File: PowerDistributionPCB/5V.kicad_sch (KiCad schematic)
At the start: 1 part

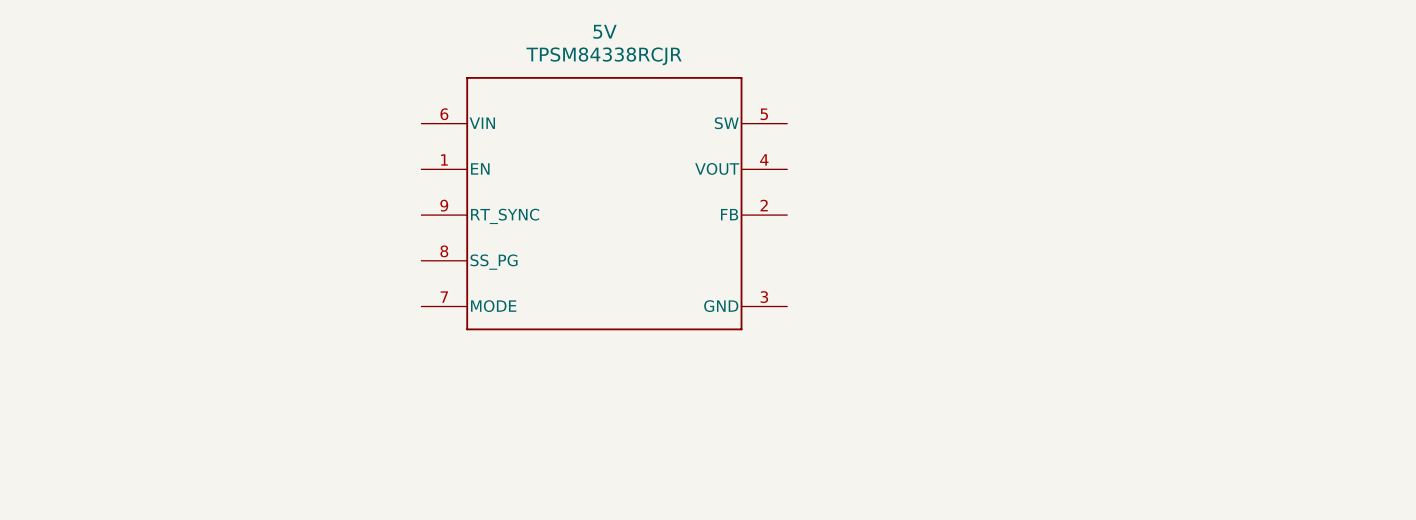
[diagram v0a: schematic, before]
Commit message: 5V buck converter
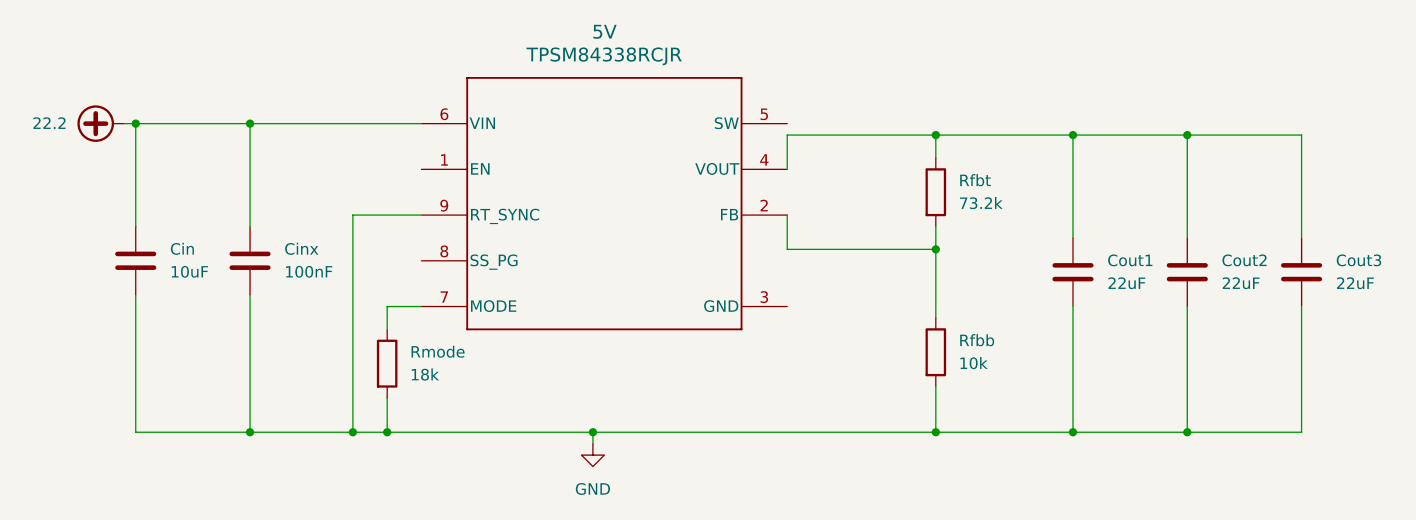
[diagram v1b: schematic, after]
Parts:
- added Cin: 10uF, symbol Device:C
- added Cinx: 100nF, symbol Device:C
- added Cout1, Cout2, Cout3: 22uF, symbol Device:C
- added Rfbb: 10k, symbol Device:R
- added Rfbt: 73.2k, symbol Device:R
- added Rmode: 18k, symbol Device:R
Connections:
- net at 5V.2 (FB): now also Rfbb.1, Rfbt.2
- net at 5V.4 (VOUT): now also Cout1.1, Cout2.1, Cout3.1, Rfbt.1
- net 22.2: now reaches 5V.6 (VIN)
- net 22.2: now also Cin.1, Cinx.1
- net at 5V.7 (MODE): now also Rmode.1
- net GND: now reaches 5V.9 (RT_SYNC)
- net GND: now also Cin.2, Cinx.2, Cout1.2, Cout2.2, Cout3.2, Rfbb.2, Rmode.2
